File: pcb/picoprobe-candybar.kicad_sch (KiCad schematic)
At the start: 25 parts, among them J1 Conn_IDC_Cable, J2 SWD-UART_PicoprobeCandybar, Q1 BSS806N, SW1 SLW-156646-5A-N-D, SW2 SW-R1-1A-E-1-0, U1 74AUP1T17, U2 74AUP1T17

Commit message: Associate SW2 with unconventional footprint
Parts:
- SW2: footprint (none) -> ProjectFootprints_PicoprobeCandybar:SW_Rocker_SPST_QuickConnect_P10.8mm_SW-R1-1X-E-XX-0_Retrofit-SMD-Horizontal
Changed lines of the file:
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@@
 			)
 		)
-		(property "Footprint" ""
+		(property "Footprint" "ProjectFootprints_PicoprobeCandybar:SW_Rocker_SPST_QuickConnect_P10.8mm_SW-R1-1X-E-XX-0_Retrofit-SMD-Horizontal"
 			(at 50.8 118.11 0)
 			(effects

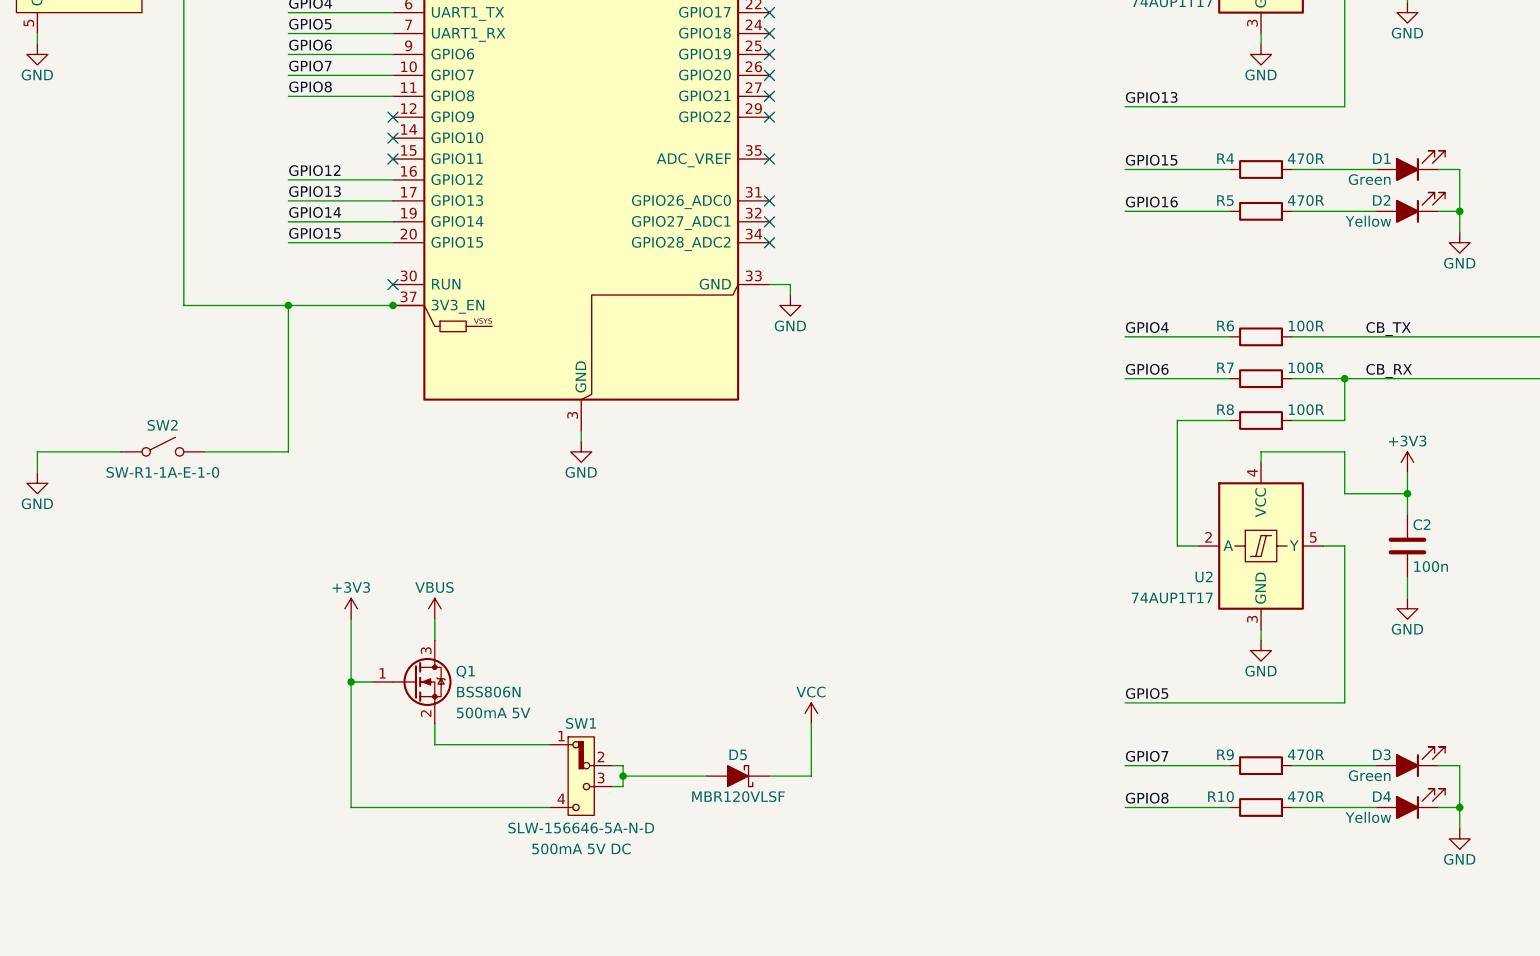
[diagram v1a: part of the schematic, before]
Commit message: Reindex symbols
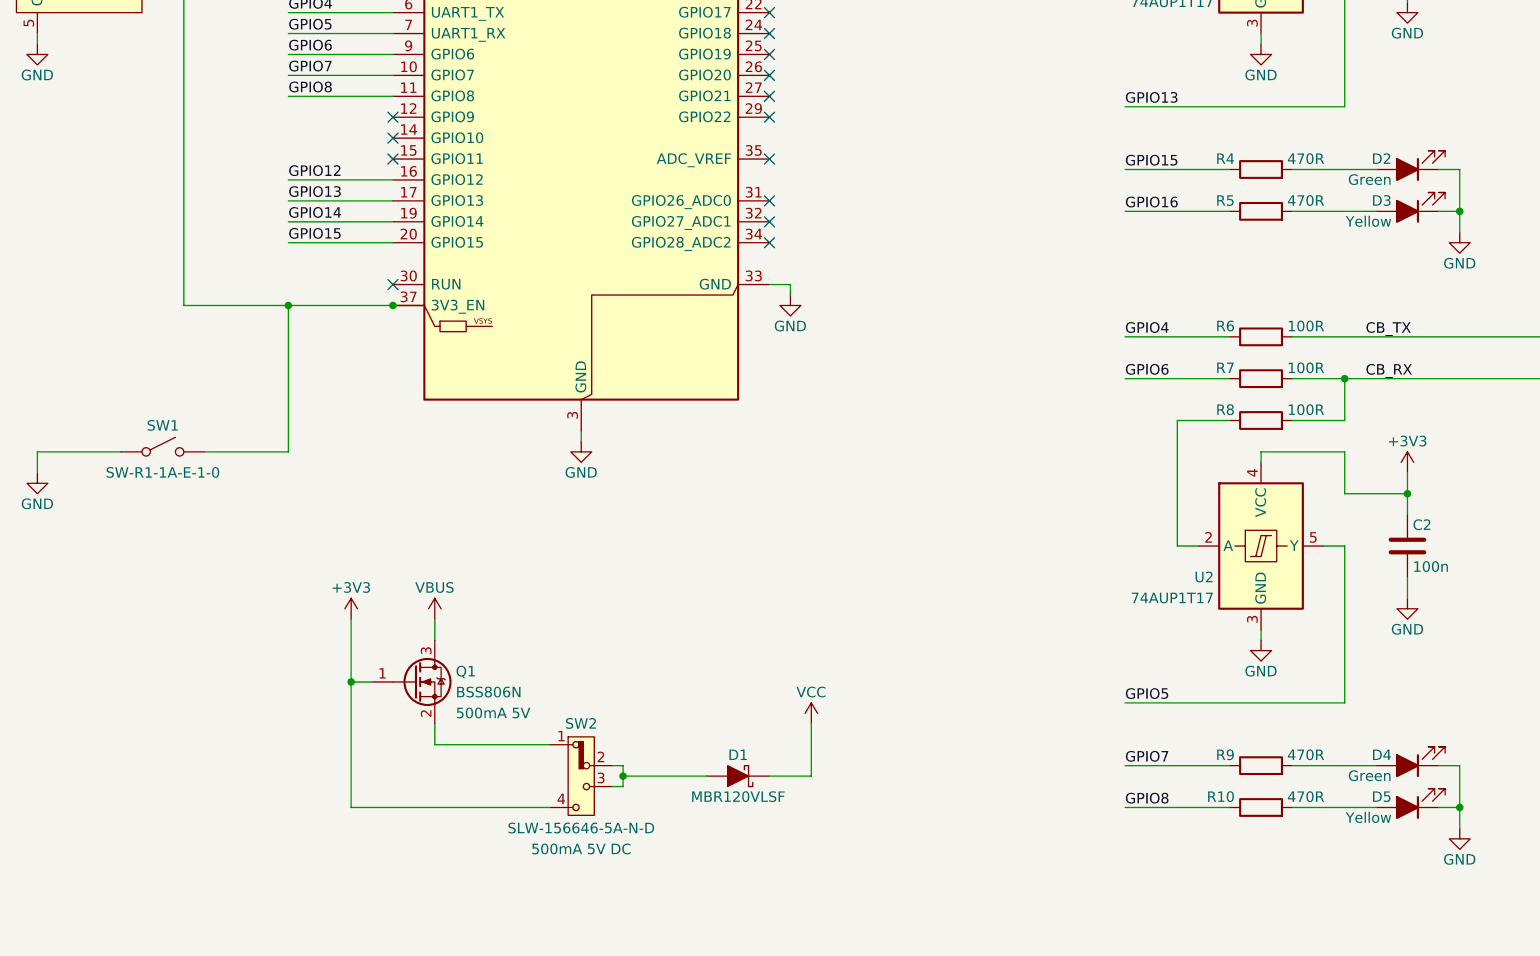
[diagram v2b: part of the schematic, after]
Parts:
- renumbered D5 to D1, D1 to D2, D2 to D3, D3 to D4, D4 to D5, SW2 to SW1, SW1 to SW2
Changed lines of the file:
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@@
 		(on_board yes)
 		(dnp no)
-		(property "Reference" "#PWR07"
+		(property "Reference" "#PWR011"
 			(at 184.15 147.32 0)
 			(effects
@@
 			(project "picoprobe-candybar"
 				(path "/73798b73-b835-4423-abd2-5bd613a215bf"
-					(reference "#PWR07")
+					(reference "#PWR011")
 					(unit 1)
 				)
@@
 		(on_board yes)
 		(dnp no)
-		(property "Reference" "SW2"
+		(property "Reference" "SW1"
 			(at 50.8 114.935 0)
 			(effects
@@
 			(project ""
 				(path "/73798b73-b835-4423-abd2-5bd613a215bf"
-					(reference "SW2")
+					(reference "SW1")
 					(unit 1)
 				)
@@
 		(on_board yes)
 		(dnp no)
-		(property "Reference" "#PWR013"
+		(property "Reference" "#PWR08"
 			(at 127 105.41 0)
 			(effects
@@
 			(project "picoprobe-candybar"
 				(path "/73798b73-b835-4423-abd2-5bd613a215bf"
-					(reference "#PWR013")
+					(reference "#PWR08")
 					(unit 1)
 				)
@@
 		(on_board yes)
 		(dnp no)
-		(property "Reference" "#PWR015"
+		(property "Reference" "#PWR09"
 			(at 129.54 154.94 0)
 			(effects
@@
 			(project "picoprobe-candybar"
 				(path "/73798b73-b835-4423-abd2-5bd613a215bf"
-					(reference "#PWR015")
+					(reference "#PWR09")
 					(unit 1)
 				)
@@
 		(on_board yes)
 		(dnp no)
-		(property "Reference" "#PWR016"
+		(property "Reference" "#PWR020"
 			(at 304.8 194.31 0)
 			(effects
@@
 			(project "picoprobe-candybar"
 				(path "/73798b73-b835-4423-abd2-5bd613a215bf"
-					(reference "#PWR016")
+					(reference "#PWR020")
 					(unit 1)
 				)
@@
 		(on_board yes)
 		(dnp no)
-		(property "Reference" "#PWR03"
+		(property "Reference" "#PWR013"
 			(at 201.93 69.85 0)
 			(effects
@@
 			(project "picoprobe-candybar"
 				(path "/73798b73-b835-4423-abd2-5bd613a215bf"
-					(reference "#PWR03")
+					(reference "#PWR013")
 					(unit 1)
 				)
@@
 		(on_board yes)
 		(dnp no)
-		(property "Reference" "D1"
+		(property "Reference" "D2"
 			(at 200.025 82.55 0)
 			(effects
@@
 			(project ""
 				(path "/73798b73-b835-4423-abd2-5bd613a215bf"
-					(reference "D1")
+					(reference "D2")
 					(unit 1)
 				)
@@
 		(on_board yes)
 		(dnp no)
-		(property "Reference" "D2"
+		(property "Reference" "D3"
 			(at 200.025 87.63 0)
 			(effects
@@
 			(project "picoprobe-candybar"
 				(path "/73798b73-b835-4423-abd2-5bd613a215bf"
-					(reference "D2")
+					(reference "D3")
 					(unit 1)
 				)
@@
 		(on_board yes)
 		(dnp no)
-		(property "Reference" "#PWR019"
+		(property "Reference" "#PWR03"
 			(at 73.66 142.24 0)
 			(effects
@@
 			(project "picoprobe-candybar"
 				(path "/73798b73-b835-4423-abd2-5bd613a215bf"
-					(reference "#PWR019")
+					(reference "#PWR03")
 					(unit 1)
 				)
@@
 		(on_board yes)
 		(dnp no)
-		(property "Reference" "#PWR06"
+		(property "Reference" "#PWR010"
 			(at 184.15 74.93 0)
 			(effects
@@
 			(project "picoprobe-candybar"
 				(path "/73798b73-b835-4423-abd2-5bd613a215bf"
-					(reference "#PWR06")
+					(reference "#PWR010")
 					(unit 1)
 				)
@@
 		(on_board yes)
 		(dnp no)
-		(property "Reference" "D4"
+		(property "Reference" "D5"
 			(at 200.025 160.02 0)
 			(effects
@@
 			(project "picoprobe-candybar"
 				(path "/73798b73-b835-4423-abd2-5bd613a215bf"
-					(reference "D4")
+					(reference "D5")
 					(unit 1)
 				)
@@
 		(on_board yes)
 		(dnp no)
-		(property "Reference" "#PWR012"
+		(property "Reference" "#PWR06"
 			(at 101.6 123.19 0)
 			(effects
@@
 			(project "picoprobe-candybar"
 				(path "/73798b73-b835-4423-abd2-5bd613a215bf"
-					(reference "#PWR012")
+					(reference "#PWR06")
 					(unit 1)
 				)
@@
 		(on_board yes)
 		(dnp no)
-		(property "Reference" "#PWR014"
+		(property "Reference" "#PWR04"
 			(at 83.82 142.24 0)
 			(effects
@@
 			(project "picoprobe-candybar"
 				(path "/73798b73-b835-4423-abd2-5bd613a215bf"
-					(reference "#PWR014")
+					(reference "#PWR04")
 					(unit 1)
 				)
@@
 		(on_board yes)
 		(dnp no)
-		(property "Reference" "#PWR09"
+		(property "Reference" "#PWR015"
 			(at 201.93 142.24 0)
 			(effects
@@
 			(project "picoprobe-candybar"
 				(path "/73798b73-b835-4423-abd2-5bd613a215bf"
-					(reference "#PWR09")
+					(reference "#PWR015")
 					(unit 1)
 				)
@@
 		(on_board yes)
 		(dnp no)
-		(property "Reference" "#PWR017"
+		(property "Reference" "#PWR07"
 			(at 106.68 38.1 0)
 			(effects
@@
 			(project "picoprobe-candybar"
 				(path "/73798b73-b835-4423-abd2-5bd613a215bf"
-					(reference "#PWR017")
+					(reference "#PWR07")
 					(unit 1)
 				)
@@
 		(on_board yes)
 		(dnp no)
-		(property "Reference" "#PWR04"
+		(property "Reference" "#PWR012"
 			(at 201.93 52.07 0)
 			(effects
@@
 			(project ""
 				(path "/73798b73-b835-4423-abd2-5bd613a215bf"
-					(reference "#PWR04")
+					(reference "#PWR012")
 					(unit 1)
 				)
@@
 		(on_board yes)
 		(dnp no)
-		(property "Reference" "D3"
+		(property "Reference" "D4"
 			(at 200.025 154.94 0)
 			(effects
@@
 			(project "picoprobe-candybar"
 				(path "/73798b73-b835-4423-abd2-5bd613a215bf"
-					(reference "D3")
+					(reference "D4")
 					(unit 1)
 				)
@@
 		(on_board yes)
 		(dnp no)
-		(property "Reference" "#PWR02"
+		(property "Reference" "#PWR019"
 			(at 264.16 59.69 0)
 			(effects
@@
 			(project ""
 				(path "/73798b73-b835-4423-abd2-5bd613a215bf"
-					(reference "#PWR02")
+					(reference "#PWR019")
 					(unit 1)
 				)
@@
 		(on_board yes)
 		(dnp no)
-		(property "Reference" "#PWR05"
+		(property "Reference" "#PWR016"
 			(at 208.28 97.79 0)
 			(effects
@@
 			(project ""
 				(path "/73798b73-b835-4423-abd2-5bd613a215bf"
-					(reference "#PWR05")
+					(reference "#PWR016")
 					(unit 1)
 				)
@@
 		(on_board yes)
 		(dnp no)
-		(property "Reference" "#PWR018"
+		(property "Reference" "#PWR01"
 			(at 35.56 74.93 0)
 			(effects
@@
 			(project "picoprobe-candybar"
 				(path "/73798b73-b835-4423-abd2-5bd613a215bf"
-					(reference "#PWR018")
+					(reference "#PWR01")
 					(unit 1)
 				)
@@
 		(on_board yes)
 		(dnp no)
-		(property "Reference" "#PWR011"
+		(property "Reference" "#PWR05"
 			(at 96.52 38.1 0)
 			(effects
@@
 			(project "picoprobe-candybar"
 				(path "/73798b73-b835-4423-abd2-5bd613a215bf"
-					(reference "#PWR011")
+					(reference "#PWR05")
 					(unit 1)
 				)
@@
 		(on_board yes)
 		(dnp no)
-		(property "Reference" "#PWR01"
+		(property "Reference" "#PWR018"
 			(at 222.25 80.01 0)
 			(effects
@@
 			(project ""
 				(path "/73798b73-b835-4423-abd2-5bd613a215bf"
-					(reference "#PWR01")
+					(reference "#PWR018")
 					(unit 1)
 				)
@@
 		(on_board yes)
 		(dnp no)
-		(property "Reference" "SW1"
+		(property "Reference" "SW2"
 			(at 101.6 151.13 0)
 			(effects
@@
 			(project ""
 				(path "/73798b73-b835-4423-abd2-5bd613a215bf"
-					(reference "SW1")
+					(reference "SW2")
 					(unit 1)
 				)
@@
 		(on_board yes)
 		(dnp no)
-		(property "Reference" "#PWR08"
+		(property "Reference" "#PWR014"
 			(at 201.93 124.46 0)
 			(effects
@@
 			(project "picoprobe-candybar"
 				(path "/73798b73-b835-4423-abd2-5bd613a215bf"
-					(reference "#PWR08")
+					(reference "#PWR014")
 					(unit 1)
 				)
@@
 		(on_board yes)
 		(dnp no)
-		(property "Reference" "#PWR010"
+		(property "Reference" "#PWR017"
 			(at 208.28 170.18 0)
 			(effects
@@
 			(project "picoprobe-candybar"
 				(path "/73798b73-b835-4423-abd2-5bd613a215bf"
-					(reference "#PWR010")
+					(reference "#PWR017")
 					(unit 1)
 				)
@@
 		(on_board yes)
 		(dnp no)
-		(property "Reference" "D5"
+		(property "Reference" "D1"
 			(at 120.65 154.94 0)
 			(effects
@@
 			(project "picoprobe-candybar"
 				(path "/73798b73-b835-4423-abd2-5bd613a215bf"
-					(reference "D5")
+					(reference "D1")
 					(unit 1)
 				)
@@
 		(on_board yes)
 		(dnp no)
-		(property "Reference" "#PWR020"
+		(property "Reference" "#PWR02"
 			(at 35.56 127 0)
 			(effects
@@
 			(project "picoprobe-candybar"
 				(path "/73798b73-b835-4423-abd2-5bd613a215bf"
-					(reference "#PWR020")
+					(reference "#PWR02")
 					(unit 1)
 				)
